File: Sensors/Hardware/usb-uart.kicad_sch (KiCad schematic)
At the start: 16 parts

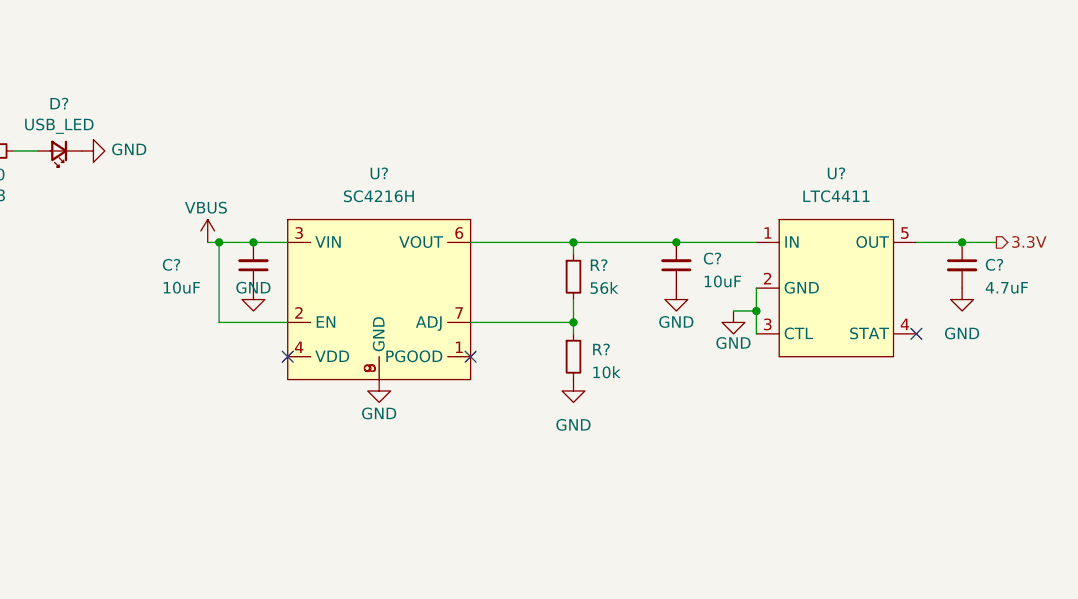
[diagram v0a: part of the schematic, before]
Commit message: added template changes
Moved power to seperate file
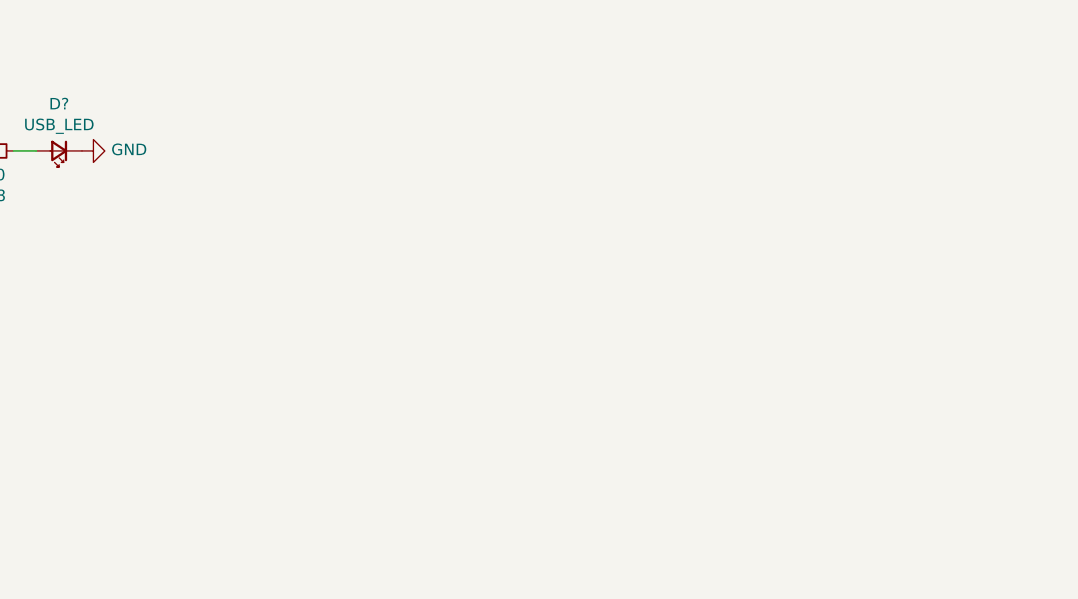
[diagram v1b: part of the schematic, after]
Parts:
- removed C? (x2): 10uF, Capacitor_SMD:C_0603_1608Metric, symbol Device:C_Small
- removed C?: 4.7uF, Capacitor_SMD:C_0603_1608Metric, symbol Device:C_Small
- removed R?: 10k, Resistor_SMD:R_0402_1005Metric, symbol Device:R_Small
- removed R?: 56k, Resistor_SMD:R_0402_1005Metric, symbol Device:R_Small
- removed U?: LTC4411, Package_TO_SOT_SMD:SOT-23-5, symbol iclr:LTC4411
- removed U?: SC4216H, iclr:SOIC127P599X175-9N, symbol iclr:RT9025-25GSP
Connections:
- no-connect marks 5 -> 2

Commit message: fp assignments
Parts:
- gave numbers to parts that had none: 5
- renumbered R18 to R68, TP18 to TP_DATA+1, TP17 to TP_DATA-1, TP19 to TP_VBUS1
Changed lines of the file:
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@@
   (symbol (lib_id "power:GND") (at 127 96.52 90) (unit 1)
     (in_bom yes) (on_board yes)
-    (property "Reference" "#PWR?" (id 0) (at 133.35 96.52 0)
+    (property "Reference" "#PWR0148" (id 0) (at 133.35 96.52 0)
       (effects (font (size 1.27 1.27)) hide)
     )
@@
   (symbol (lib_id "Device:R_Small") (at 123.19 99.06 270) (unit 1)
     (in_bom yes) (on_board yes)
-    (property "Reference" "R?" (id 0) (at 129.54 100.33 90))
+    (property "Reference" "R67" (id 0) (at 129.54 100.33 90))
     (property "Value" "5.1k" (id 1) (at 129.54 102.6414 90))
     (property "Footprint" "Resistor_SMD:R_0402_1005Metric" (id 2) (at 123.19 99.06 0)
@@
   (symbol (lib_id "Device:R_Small") (at 123.19 93.98 90) (unit 1)
     (in_bom yes) (on_board yes)
-    (property "Reference" "R?" (id 0) (at 123.19 89.0016 90))
+    (property "Reference" "R66" (id 0) (at 123.19 89.0016 90))
     (property "Value" "5.1k" (id 1) (at 123.19 91.313 90))
     (property "Footprint" "Resistor_SMD:R_0402_1005Metric" (id 2) (at 123.19 93.98 0)
@@
   (symbol (lib_id "power:GND") (at 96.52 130.81 0) (unit 1)
     (in_bom yes) (on_board yes)
-    (property "Reference" "#PWR?" (id 0) (at 96.52 137.16 0)
+    (property "Reference" "#PWR0146" (id 0) (at 96.52 137.16 0)
       (effects (font (size 1.27 1.27)) hide)
     )
@@
   (symbol (lib_id "Connector:USB_C_Receptacle_USB2.0") (at 100.33 104.14 0) (unit 1)
     (in_bom yes) (on_board yes)
-    (property "Reference" "J?" (id 0) (at 103.0478 82.1182 0))
+    (property "Reference" "J15" (id 0) (at 103.0478 82.1182 0))
     (property "Value" "USB_C_Receptacle_USB2.0" (id 1) (at 103.0478 84.4296 0))
     (property "Footprint" "Connector_USB:USB_C_Receptacle_GCT_USB4085" (id 2) (at 104.14 104.14 0)
@@
   (symbol (lib_id "power:GND") (at 132.08 144.78 0) (unit 1)
     (in_bom yes) (on_board yes)
-    (property "Reference" "#PWR?" (id 0) (at 132.08 151.13 0)
+    (property "Reference" "#PWR0149" (id 0) (at 132.08 151.13 0)
       (effects (font (size 1.27 1.27)) hide)
     )
@@
   (symbol (lib_id "Power_Protection:SP0503BAHT") (at 132.08 139.7 0) (unit 1)
     (in_bom yes) (on_board yes)
-    (property "Reference" "D?" (id 0) (at 137.287 138.5316 0)
+    (property "Reference" "D2" (id 0) (at 137.287 138.5316 0)
       (effects (font (size 1.27 1.27)) (justify left))
     )
@@
   (symbol (lib_id "power:VBUS") (at 116.84 85.09 0) (unit 1)
     (in_bom yes) (on_board yes)
-    (property "Reference" "#PWR?" (id 0) (at 116.84 88.9 0)
+    (property "Reference" "#PWR0147" (id 0) (at 116.84 88.9 0)
       (effects (font (size 1.27 1.27)) hide)
     )
@@
   (symbol (lib_id "Connector:TestPoint") (at 52.07 99.06 270) (unit 1)
     (in_bom yes) (on_board yes)
-    (property "Reference" "TP_DATA-?" (id 0) (at 56.8452 97.8916 90)
+    (property "Reference" "TP_DATA-1" (id 0) (at 56.8452 97.8916 90)
       (effects (font (size 1.27 1.27)) (justify left))
     )
@@
   (symbol (lib_id "Connector:TestPoint") (at 52.07 104.14 270) (unit 1)
     (in_bom yes) (on_board yes)
-    (property "Reference" "TP_DATA+?" (id 0) (at 56.8452 102.9716 90)
+    (property "Reference" "TP_DATA+1" (id 0) (at 56.8452 102.9716 90)
       (effects (font (size 1.27 1.27)) (justify left))
     )
@@
   (symbol (lib_id "Connector:TestPoint") (at 52.07 109.22 270) (unit 1)
     (in_bom yes) (on_board yes)
-    (property "Reference" "TP_VBUS?" (id 0) (at 56.8452 108.0516 90)
+    (property "Reference" "TP_VBUS1" (id 0) (at 56.8452 108.0516 90)
       (effects (font (size 1.27 1.27)) (justify left))
     )
@@
   (symbol (lib_id "Device:LED_Small") (at 162.56 92.71 180) (unit 1)
     (in_bom yes) (on_board yes)
-    (property "Reference" "USBLED?" (id 0) (at 162.56 87.503 0))
+    (property "Reference" "USBLED1" (id 0) (at 162.56 87.503 0))
     (property "Value" "USB_LED" (id 1) (at 162.56 89.8144 0))
     (property "Footprint" "LED_SMD:LED_0603_1608Metric" (id 2) (at 162.56 92.71 90)
@@
   (symbol (lib_id "Device:R_Small") (at 154.94 92.71 90) (unit 1)
     (in_bom yes) (on_board yes)
-    (property "Reference" "R?" (id 0) (at 154.94 97.6884 90))
+    (property "Reference" "R68" (id 0) (at 154.94 97.6884 90))
     (property "Value" "470" (id 1) (at 154.94 95.377 90))
     (property "Footprint" "Resistor_SMD:R_0402_1005Metric" (id 2) (at 154.94 92.71 0)
@@
   (symbol (lib_id "power:GND") (at 165.1 92.71 90) (unit 1)
     (in_bom yes) (on_board yes)
-    (property "Reference" "#PWR?" (id 0) (at 171.45 92.71 0)
+    (property "Reference" "#PWR0151" (id 0) (at 171.45 92.71 0)
       (effects (font (size 1.27 1.27)) hide)
     )
@@
   (symbol (lib_id "power:VBUS") (at 152.4 92.71 90) (unit 1)
     (in_bom yes) (on_board yes)
-    (property "Reference" "#PWR?" (id 0) (at 156.21 92.71 0)
-      (effects (font (size 1.27 1.27)) hide)
-    )
+    (property "Reference" "#PWR0150" (id 0) (at 156.21 92.71 0)
+      (effects (font (size 1.27 1.27)) hide)
+    )

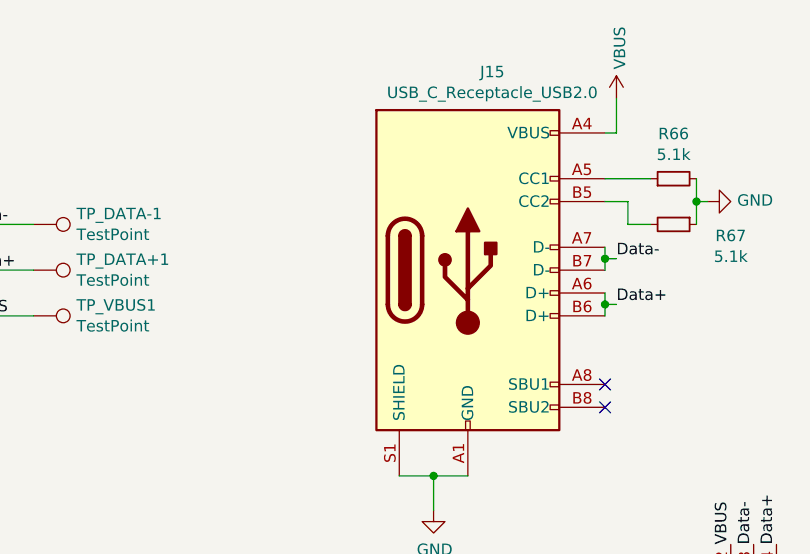
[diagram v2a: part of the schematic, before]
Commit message: ADC connections and KiCAD version update
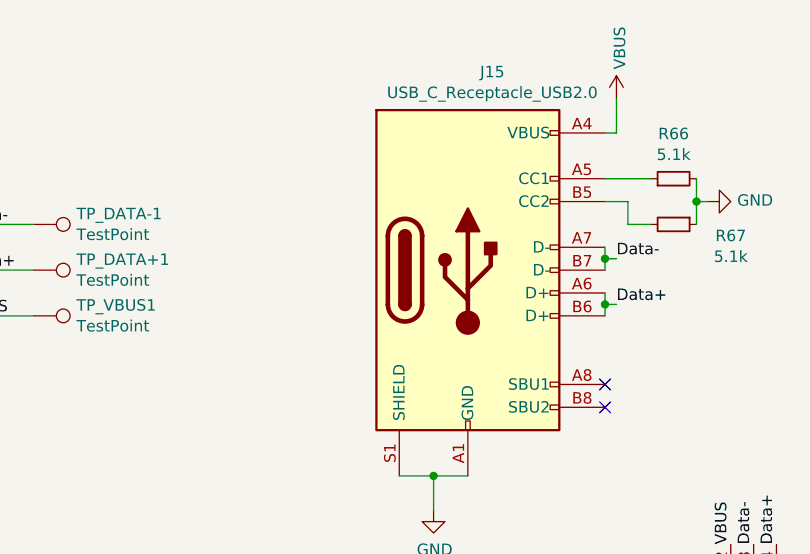
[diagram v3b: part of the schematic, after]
